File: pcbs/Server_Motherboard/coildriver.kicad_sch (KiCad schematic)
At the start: 4 parts, among them IC1 BTM9011EPXUMA1

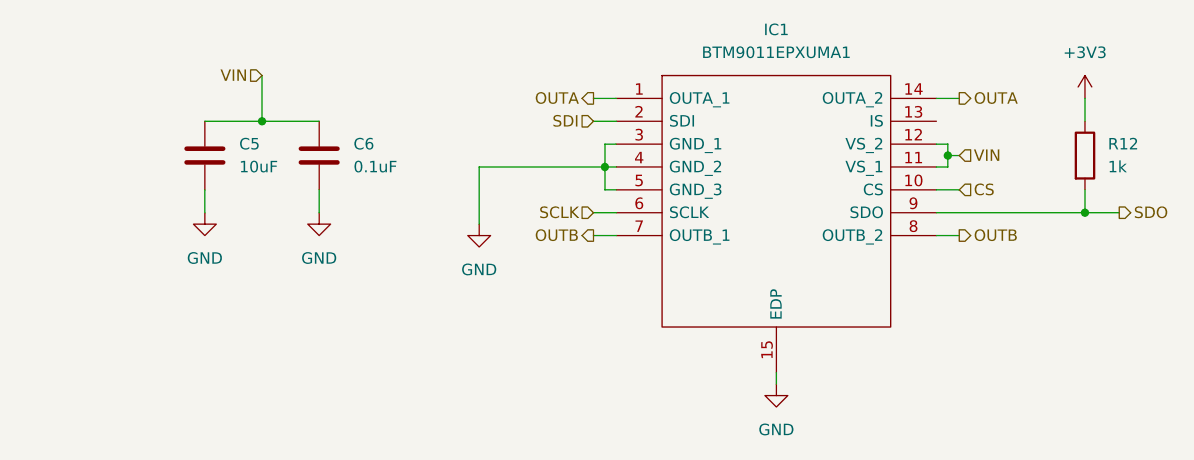
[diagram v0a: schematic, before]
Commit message: mostly finished server pcb, added pogo charge pins to bots, started charge case pcb
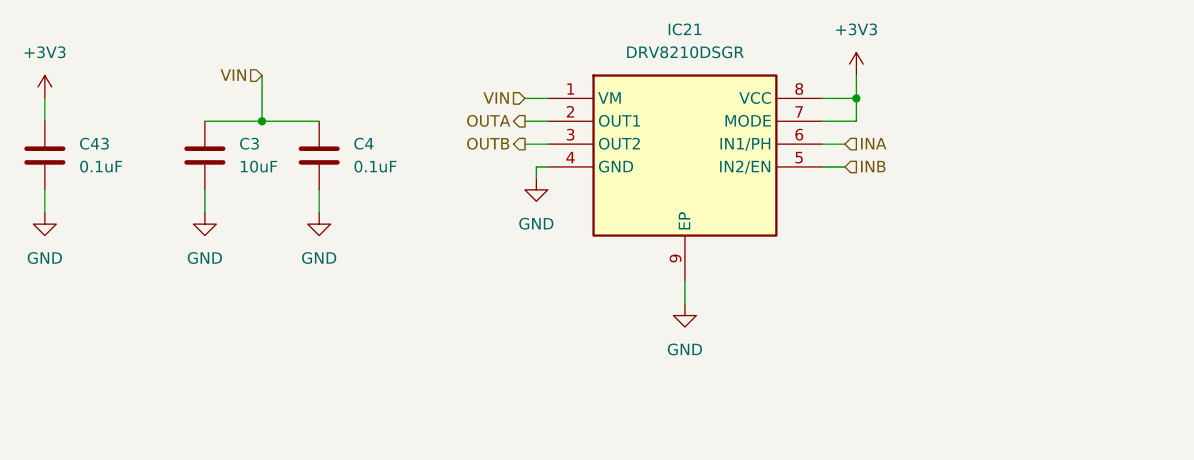
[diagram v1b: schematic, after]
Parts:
- removed IC1: BTM9011EPXUMA1, SOP65P600X115-15N, symbol SamacSys_Parts:BTM9011EPXUMA1
- removed R12: 1k, Resistor_SMD:R_0603_1608Metric, symbol Device:R
- added C43: 0.1uF, Capacitor_SMD:C_0402_1005Metric, symbol Device:C
- added IC21: DRV8210DSGR, SON50P200X200X80-9N, symbol SamacSys_Parts:DRV8210DSGR
- C4: renamed from C6; footprint Capacitor_SMD:C_0603_1608Metric -> Capacitor_SMD:C_0402_1005Metric
- renumbered C5 to C3
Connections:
- net +3V3: now also C43.1, IC21.7 (MODE), IC21.8 (VCC)
- net GND: now also C43.2, IC21.4 (GND), IC21.9 (EP)
- net OUTA: now also IC21.2 (OUT1)
- net OUTB: now also IC21.3 (OUT2)
- net VIN: now also IC21.1 (VM)
- new net INA: IC21.6 (IN1/PH)
- new net INB: IC21.5 (IN2/EN)
